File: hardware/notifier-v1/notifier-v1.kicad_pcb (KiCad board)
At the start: 4 copper layers, 50 x 36 mm, 32 parts, among them J1 USB-C, J2 GC9A01, SW1 RESET, SW2 BOOT, SW3 BUTTON, U1 ESP32-S3-WROOM-1-N8R2, U2 USBLC6-2SC6, U3 AMS1117-3.3, U4 BME688

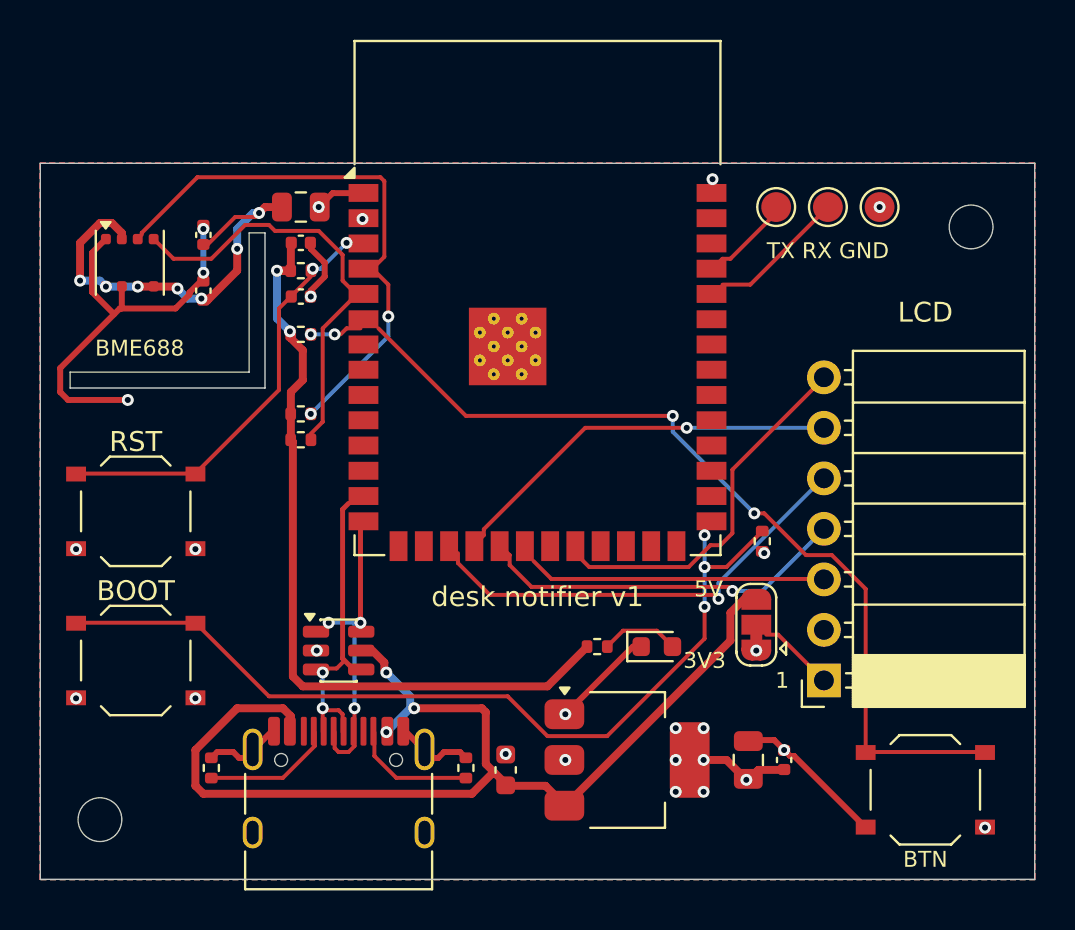
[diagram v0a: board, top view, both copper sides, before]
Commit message: hardware: notifier-v1 rev after design review (buck, sensor peninsula, no via-in-pad)
Review findings applied: TLV62569 buck instead of AMS1117 (0.6 W into the sensor), 500 mA
polyfuse, BME688 on a peninsula with the neck away from the module, custom DRC rule and
KRT settings against vias in SMD pads, signals on the outer layers only, display socket
face past the edge with pin names, more debug pads, antenna strip without pours/vias.
Safe cleanup of router leftovers, one-command pipeline, order checklist.

Co-Authored-By: Claude Opus 5.5 <noreply@anthropic.com>
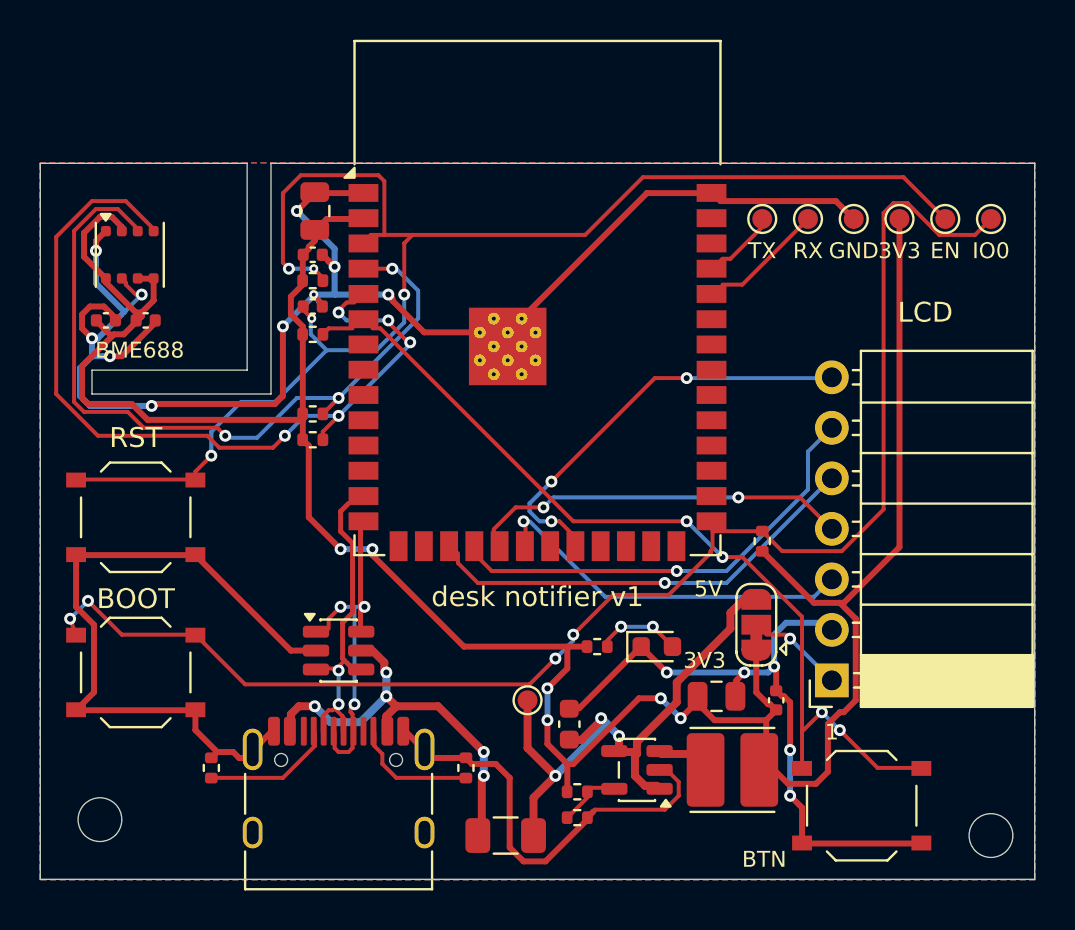
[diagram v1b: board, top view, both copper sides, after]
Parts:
- added F1: 500mA, Fuse:Fuse_1206_3216Metric, F.Cu at (123.4, 133.8)
- added L1: 2.2u, Inductor_SMD:L_Cenker_CKCS4030, F.Cu at (134.8, 130.5)
- added R10: 22k, Resistor_SMD:R_0402_1005Metric, F.Cu at (127.0, 132.9)
- added R9: 100k, Resistor_SMD:R_0402_1005Metric, F.Cu at (127.0, 131.6)
- added TP4: 3V3, TestPoint:TestPoint_Pad_D1.0mm, F.Cu at (143.2, 102.8)
- added TP5: EN, TestPoint:TestPoint_Pad_D1.0mm, F.Cu at (145.5, 102.8)
- added TP6: IO0, TestPoint:TestPoint_Pad_D1.0mm, F.Cu at (147.8, 102.8)
- added TP7: VBUS, TestPoint:TestPoint_Pad_D1.0mm, F.Cu at (124.5, 127.0)
- R3: value 1k -> 4.7k
- TP1, TP2, TP3: footprint TestPoint:TestPoint_Pad_D1.5mm -> TestPoint:TestPoint_Pad_D1.0mm
- U3: value AMS1117-3.3 -> TLV62569; footprint Package_TO_SOT_SMD:SOT-223-3_TabPin2 -> Package_TO_SOT_SMD:SOT-23-5
- moved H1 30.6 mm to (147.8, 133.8)
- moved C7 6.52 mm to (103.3, 107.9), turned to 0 degrees
- moved C1 3.94 mm to (126.6, 128.2)
- moved C2 3.58 mm to (134.0, 126.8), turned to 0 degrees
- moved SW3 3.30 mm to (141.3, 132.3)
- moved C8 3.26 mm to (105.3, 107.9), turned to 0 degrees
- moved C3 3.03 mm to (137.0, 127.0)
- moved TP3 1.43 mm to (140.9, 102.8)
- moved TP2 1.17 mm to (138.6, 102.8)
- moved TP1 0.92 mm to (136.3, 102.8)
- moved C6 0.85 mm to (113.7, 104.6)
- moved C4 0.78 mm to (113.7, 107.2)
- moved R4 0.78 mm to (113.7, 105.9)
- moved C5 0.73 mm to (113.8, 102.4), turned to 90 degrees
- moved U3 0.71 mm to (130.0, 130.5), turned to 180 degrees
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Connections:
- J1 pad A4: /VBUS -> /VBUS_IN
- J1 pad A9: /VBUS -> /VBUS_IN
- J1 pad B4: /VBUS -> /VBUS_IN
- J1 pad B9: /VBUS -> /VBUS_IN
- U2 pad 5: /VBUS -> /VBUS_IN
- U3 pad 1: /GND -> /VBUS
- U3 pad 2: /+3V3 -> /GND
- U3 pad 3: /VBUS -> /SW
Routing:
- net /GND: track 50.9 -> 170.2 mm, vias 16 -> 15
- net /+3V3: track 67.8 -> 131.4 mm, vias 20 -> 6
- net /EN: track 21.3 -> 72.9 mm, vias 2 -> 5
- net /BOOT: track 45.1 -> 70.8 mm, vias 3 -> 4
- net /VBUS: track 54.4 -> 30.9 mm
- net /VBUS_IN: track 0.00 -> 20.7 mm, vias 0 -> 5
- net /I2C_SCL: track 21.5 -> 41.8 mm, vias 0 -> 5
- net /I2C_SDA: track 27.4 -> 38.7 mm, vias 2 -> 3
- net /LCD_SCLK: track 15.0 -> 18.2 mm, vias 0 -> 1
- net /FB: track 0.00 -> 2.61 mm
- net /BTN: track 46.9 -> 44.4 mm
- net /LCD_RST: track 18.6 -> 21.0 mm, vias 0 -> 3
- net /LCD_CS: track 20.2 -> 22.5 mm
- net /SW: track 0.00 -> 1.40 mm
- net /USB_DP: track 15.5 -> 16.9 mm
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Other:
- outline, holes or cut-outs redrawn
- board text added: "CS"
- board text added: "DC"
- board text added: "EN"
- board text added: "GND"
- board text added: "IO0"
- board text added: "RX"
- board text added: "SCL"
- board text added: "SDA"
- board text added: "TX"
- board text added: "VCC"
- board text removed: "TX RX GND"

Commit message: hardware: SHT40 for temperature/humidity next to the BME688
The BME688's gas heater warms it, so T/RH come from an SHT40-AD1B (C2909890, 0x44)
in the far corner of the sensor island (about 6 mm away, no pour between them).
The island grows to 11.8 mm with a wider neck; C9->VDD/VSS and SDA/SCL stubs are
hand-drawn because the SHT4x pads are 0.3 mm apart. 3V3/GND track width 0.2 mm
(planes carry the current). finish.py keeps SWIG boards alive between iterations
(an intermittent crash left a dangling via).

Co-Authored-By: Claude Opus 5.5 <noreply@anthropic.com>
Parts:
- added C9: 100n, Capacitor_SMD:C_0402_1005Metric, F.Cu at (108.8, 106.9)
- added U5: SHT40-AD1B, Sensor_Humidity:Sensirion_DFN-4_1.5x1.5mm_P0.8mm_SHT4x_NoCentralPad, F.Cu at (108.8, 108.8)
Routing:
- net /EN: track 72.9 -> 57.0 mm, vias 5 -> 4
- net /GND: track 170.2 -> 181.1 mm, vias 15 -> 11
- net /I2C_SDA: track 38.7 -> 48.9 mm
- net /BTN: track 44.4 -> 53.3 mm, vias 4 -> 2
- net /I2C_SCL: track 41.8 -> 49.7 mm
- net /LCD_MOSI: track 18.4 -> 24.9 mm
- net /VBUS: track 30.9 -> 36.7 mm, vias 3 -> 5
- net /USB_DN: track 15.7 -> 21.3 mm, vias 2 -> 3
- net /+3V3: track 131.4 -> 135.4 mm, vias 6 -> 17
- net /BOOT: track 70.8 -> 67.0 mm, vias 4 -> 3
- net /LCD_DC: track 21.9 -> 23.6 mm, vias 1 -> 2
- net /LCD_RST: track 21.0 -> 19.8 mm
- net /LCD_SCLK: track 18.2 -> 19.3 mm
- net /LCD_VCC: track 3.97 -> 4.96 mm, vias 1 -> 0
- net /VBUS_IN: track 20.7 -> 20.5 mm, vias 5 -> 3
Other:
- outline, holes or cut-outs redrawn

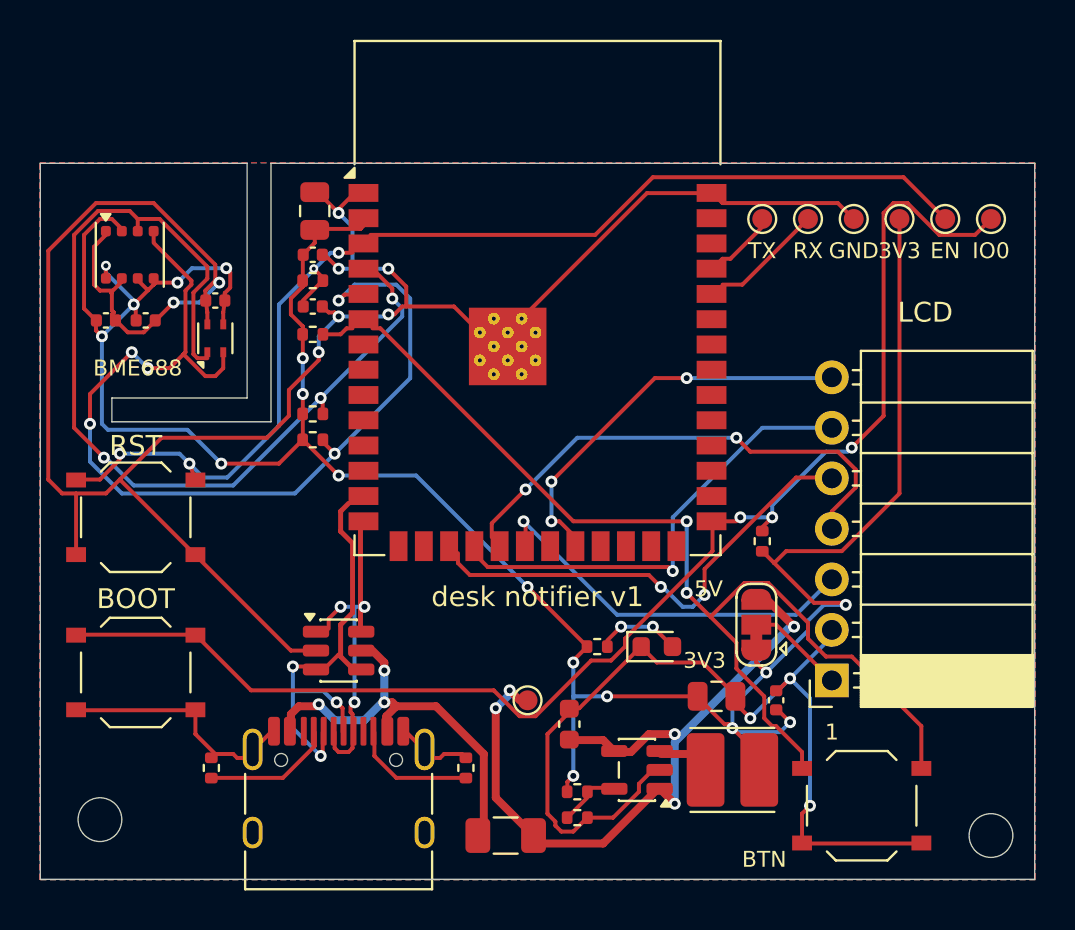
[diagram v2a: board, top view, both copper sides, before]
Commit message: Hatched In1 GND plane under the sensor island and neck as I2C return path
Co-Authored-By: Claude Opus 5.5 <noreply@anthropic.com>
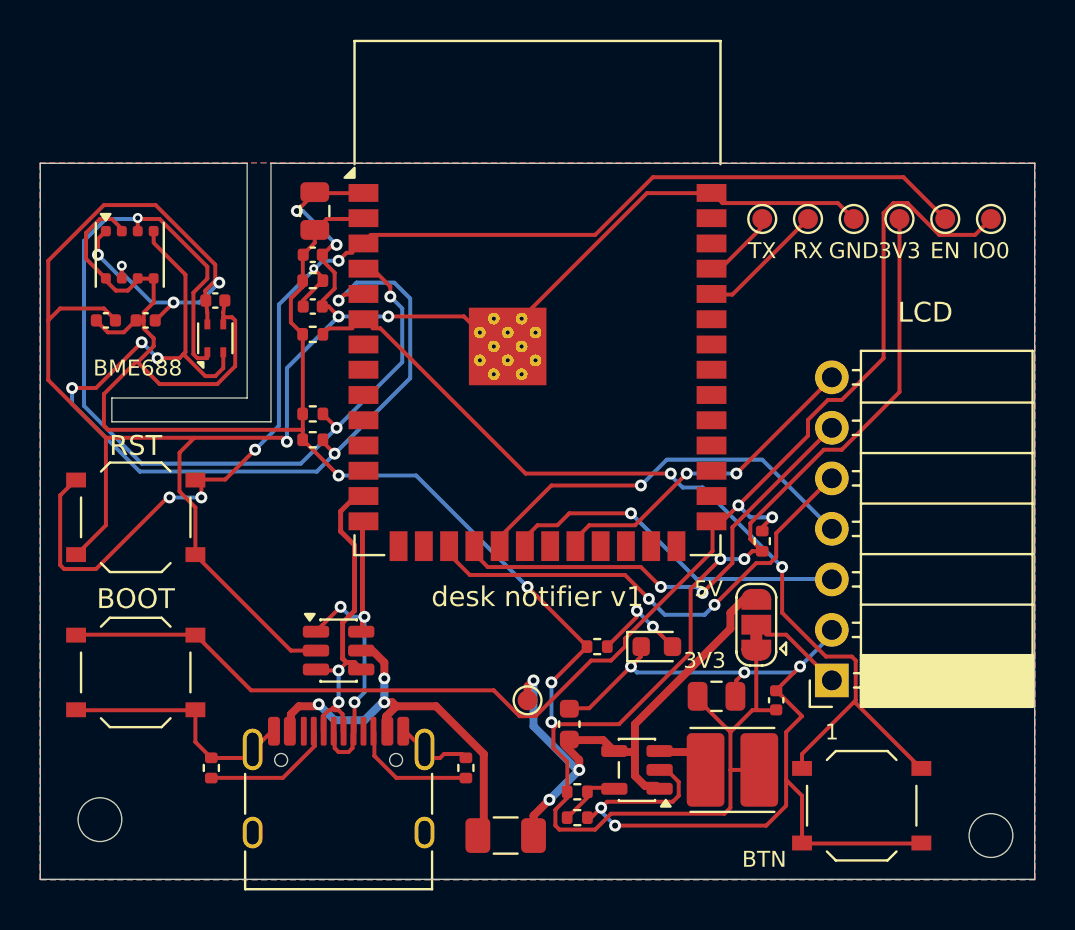
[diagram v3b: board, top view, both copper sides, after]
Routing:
- net /VBUS: track 36.7 -> 28.3 mm, vias 5 -> 3
- net /BTN: track 53.3 -> 45.3 mm
- net /+3V3: track 135.4 -> 142.6 mm, vias 17 -> 6
- net /EN: track 57.0 -> 63.3 mm, vias 4 -> 5
- net /GND: track 181.1 -> 187.3 mm, vias 11 -> 14
- net /LCD_MOSI: track 24.9 -> 19.8 mm, vias 2 -> 1
- net /USB_DN: track 21.3 -> 16.8 mm, vias 3 -> 2
- net /LCD_RST: track 19.8 -> 16.3 mm, vias 3 -> 2
- net /LCD_SCLK: track 19.3 -> 17.3 mm
- net /I2C_SDA: track 48.9 -> 47.6 mm
- net /I2C_SCL: track 49.7 -> 48.9 mm
- net /LCD_VCC: track 4.96 -> 4.25 mm
- net /RXD0: track 5.67 -> 6.37 mm
- net /LCD_CS: track 22.7 -> 23.3 mm, vias 1 -> 2
- net /LED_A: track 4.00 -> 4.67 mm
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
